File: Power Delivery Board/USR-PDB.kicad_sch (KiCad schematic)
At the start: 40 parts, among them U1 XT90, U10 Anderson PP45 Vert. 2x1, U11 Anderson PP45 Vert. 2x1, U12 Anderson PP45 Vert. 2x1, U13 TL2575HV-05IKV, U14 MCP3002-I/P, U2 Anderson PP45 Vert. 2x1, U3 Anderson PP45 Vert. 2x1, U4 Anderson PP45 Vert. 2x1, U5 Anderson PP45 Vert. 2x1, U6 Anderson PP45 Vert. 2x1, U7 LM2676T-12_NOPB

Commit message: traces added for the power delivery boards PCB
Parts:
- C1: footprint USR:CAP_WCAP-ATUL_05.0X11.0_WRE -> Capacitor_THT:CP_Radial_D10.0mm_P5.00mm
- C2, C6, C8: footprint USR:U2-K_NCH -> Capacitor_THT:CP_Radial_D10.0mm_P5.00mm
- C5: footprint USR:CAP_ATLL_06p3X15p0_WRE -> Capacitor_THT:CP_Radial_D10.0mm_P5.00mm
- C7: footprint USR:PCAP_6.3x7.7-ELECT_NCA -> Capacitor_THT:CP_Radial_D10.0mm_P5.00mm
- D1: footprint USR:SMA_DIO -> USR:DO-41_STM
- L1: footprint USR:IND_BOURNS_SRR1210 -> Inductor_THT:L_Axial_L5.3mm_D2.2mm_P10.16mm_Horizontal_Vishay_IM-1
- L2: footprint USR:IND_BOURNS_SDR1806 -> Inductor_THT:L_Axial_L7.0mm_D3.3mm_P12.70mm_Horizontal_Fastron_MICC
- L3: footprint USR:IND_BOURNS_SDR1806 -> Inductor_THT:L_Axial_L5.3mm_D2.2mm_P10.16mm_Horizontal_Vishay_IM-1
- U1: footprint (none) -> USR:AMASS_XT90PW-M_VERTICAL
- U15: footprint USR:JST-XA 2.54mm -> USR:JST-XA 4-PIN
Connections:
- no-connect marks 4 -> 16
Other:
- note removed: "create a vertical version of the AMASS_XT90PW-M for the hole sizes, reference the AMASS_XT30 vertical footprint for the layout we want"
- note removed: "find XT90 footprint"
- note removed: "use 10uH 0805 inductors, combine them into the 20uH inductor here"
- note removed: "use the 0805 SMD cap's we already have for the 100nF and 10nF cap's"
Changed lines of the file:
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@@
 		)
 	)
-	(text "use the 0805 SMD cap's we already have for \nthe 100nF and 10nF cap's"
-		(exclude_from_sim no)
-		(at 82.55 250.19 0)
-		(effects
-			(font
-				(size 1.27 1.27)
-			)
-		)
-	)
-	(text "find XT90 footprint"
-		(exclude_from_sim no)
-		(at 29.464 29.21 0)
-		(effects
-			(font
-				(size 1.27 1.27)
-			)
-		)
-	)
 	(text "3/12/2026"
 		(exclude_from_sim no)
@@
 		)
 	)
-	(text "create a vertical version of the AMASS_XT90PW-M for the hole \nsizes, reference the AMASS_XT30	vertical footprint for the\nlayout we want"
-		(exclude_from_sim no)
-		(at 78.232 32.258 0)
-		(effects
-			(font
-				(size 1.27 1.27)
-			)
-		)
-	)
 	(text "look into using JST 2.54mm XA male connectors for this"
 		(exclude_from_sim no)
@@
 		)
 	)
-	(text "use 10uH 0805 inductors, combine them into the \n20uH inductor here"
-		(exclude_from_sim no)
-		(at 373.888 186.436 0)
-		(effects
-			(font
-				(size 1.27 1.27)
-			)
-		)
-	)
 	(text "use the 3-pin JST-XA connectors to route 5V to the backplane"
 		(exclude_from_sim no)
@@
 	)
 	(no_connect
+		(at 147.32 86.36)
+	)
+	(no_connect
 		(at 135.89 220.98)
 	)
 	(no_connect
+		(at 168.91 86.36)
+	)
+	(no_connect
 		(at 152.4 101.6)
 	)
+	(no_connect
+		(at 147.32 83.82)
+	)
+	(no_connect
+		(at 147.32 36.83)
+	)
+	(no_connect
+		(at 168.91 83.82)
+	)
+	(no_connect
+		(at 147.32 41.91)
+	)
+	(no_connect
+		(at 168.91 39.37)
+	)
+	(no_connect
+		(at 147.32 39.37)
+	)
+	(no_connect
+		(at 147.32 81.28)
+	)
+	(no_connect
+		(at 168.91 81.28)
+	)
+	(no_connect
+		(at 168.91 41.91)
+	)
+	(no_connect
+		(at 168.91 36.83)
+	)
 	(wire
 		(pts
@@
 			)
 		)
-		(property "Footprint" "USR:CAP_ATLL_06p3X15p0_WRE"
+		(property "Footprint" "Capacitor_THT:CP_Radial_D10.0mm_P5.00mm"
 			(at 152.4 220.98 0)
 			(effects
@@
 			)
 		)
-		(property "Footprint" "USR:PCAP_6.3x7.7-ELECT_NCA"
+		(property "Footprint" "Capacitor_THT:CP_Radial_D10.0mm_P5.00mm"
 			(at 316.23 227.33 0)
 			(effects
@@
 			)
 		)
-		(property "Footprint" "USR:U2-K_NCH"
+		(property "Footprint" "Capacitor_THT:CP_Radial_D10.0mm_P5.00mm"
 			(at 63.5 228.6 0)
 			(effects
@@
 			)
 		)
-		(property "Footprint" "USR:CAP_WCAP-ATUL_05.0X11.0_WRE"
+		(property "Footprint" "Capacitor_THT:CP_Radial_D10.0mm_P5.00mm"
 			(at 63.5 217.17 0)
 			(effects
@@
 			)
 		)
-		(property "Footprint" "USR:U2-K_NCH"
+		(property "Footprint" "Capacitor_THT:CP_Radial_D10.0mm_P5.00mm"
 			(at 267.97 208.28 0)
 			(effects
@@
 			)
 		)
-		(property "Footprint" "USR:SMA_DIO"
+		(property "Footprint" "USR:DO-41_STM"
 			(at 88.9 232.41 0)
 			(effects
@@
 			)
 		)
-		(property "Footprint" "USR:U2-K_NCH"
+		(property "Footprint" "Capacitor_THT:CP_Radial_D10.0mm_P5.00mm"
 			(at 375.92 220.98 0)
 			(effects
@@
 			)
 		)
-		(property "Footprint" "USR:IND_BOURNS_SDR1806"
+		(property "Footprint" "Inductor_THT:L_Axial_L7.0mm_D3.3mm_P12.70mm_Horizontal_Fastron_MICC"
 			(at 287.02 215.9 0)
 			(effects
@@
 			)
 		)
-		(property "Footprint" ""
+		(property "Footprint" "USR:AMASS_XT90PW-M_VERTICAL"
 			(at 29.21 45.72 0)
 			(effects
@@
 			)
 		)
-		(property "Footprint" "USR:IND_BOURNS_SRR1210"
+		(property "Footprint" "Inductor_THT:L_Axial_L5.3mm_D2.2mm_P10.16mm_Horizontal_Vishay_IM-1"
 			(at 147.32 210.82 0)
 			(effects
@@
 			)
 		)
-		(property "Footprint" "USR:IND_BOURNS_SDR1806"
+		(property "Footprint" "Inductor_THT:L_Axial_L5.3mm_D2.2mm_P10.16mm_Horizontal_Vishay_IM-1"
 			(at 298.45 215.9 0)
 			(effects
@@
 			)
 		)
-		(property "Footprint" "USR:JST-XA 2.54mm"
+		(property "Footprint" "USR:JST-XA 4-PIN"
 			(at 375.92 53.34 0)
 			(effects

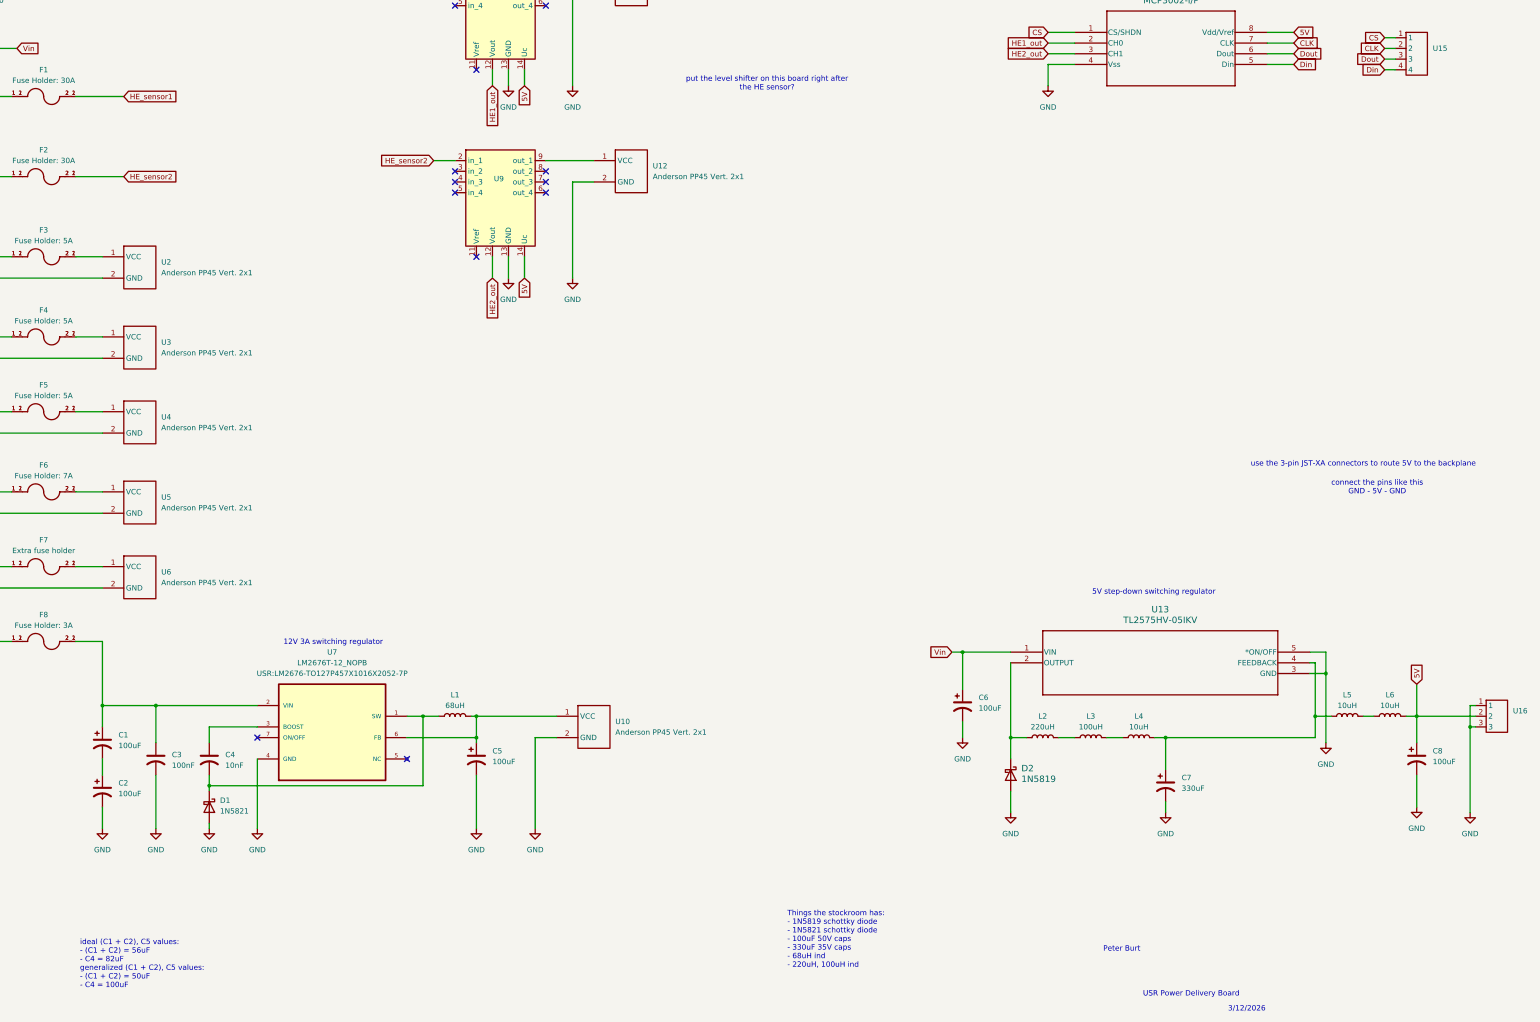
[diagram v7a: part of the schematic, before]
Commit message: Update PDB with easier-to-obtain components
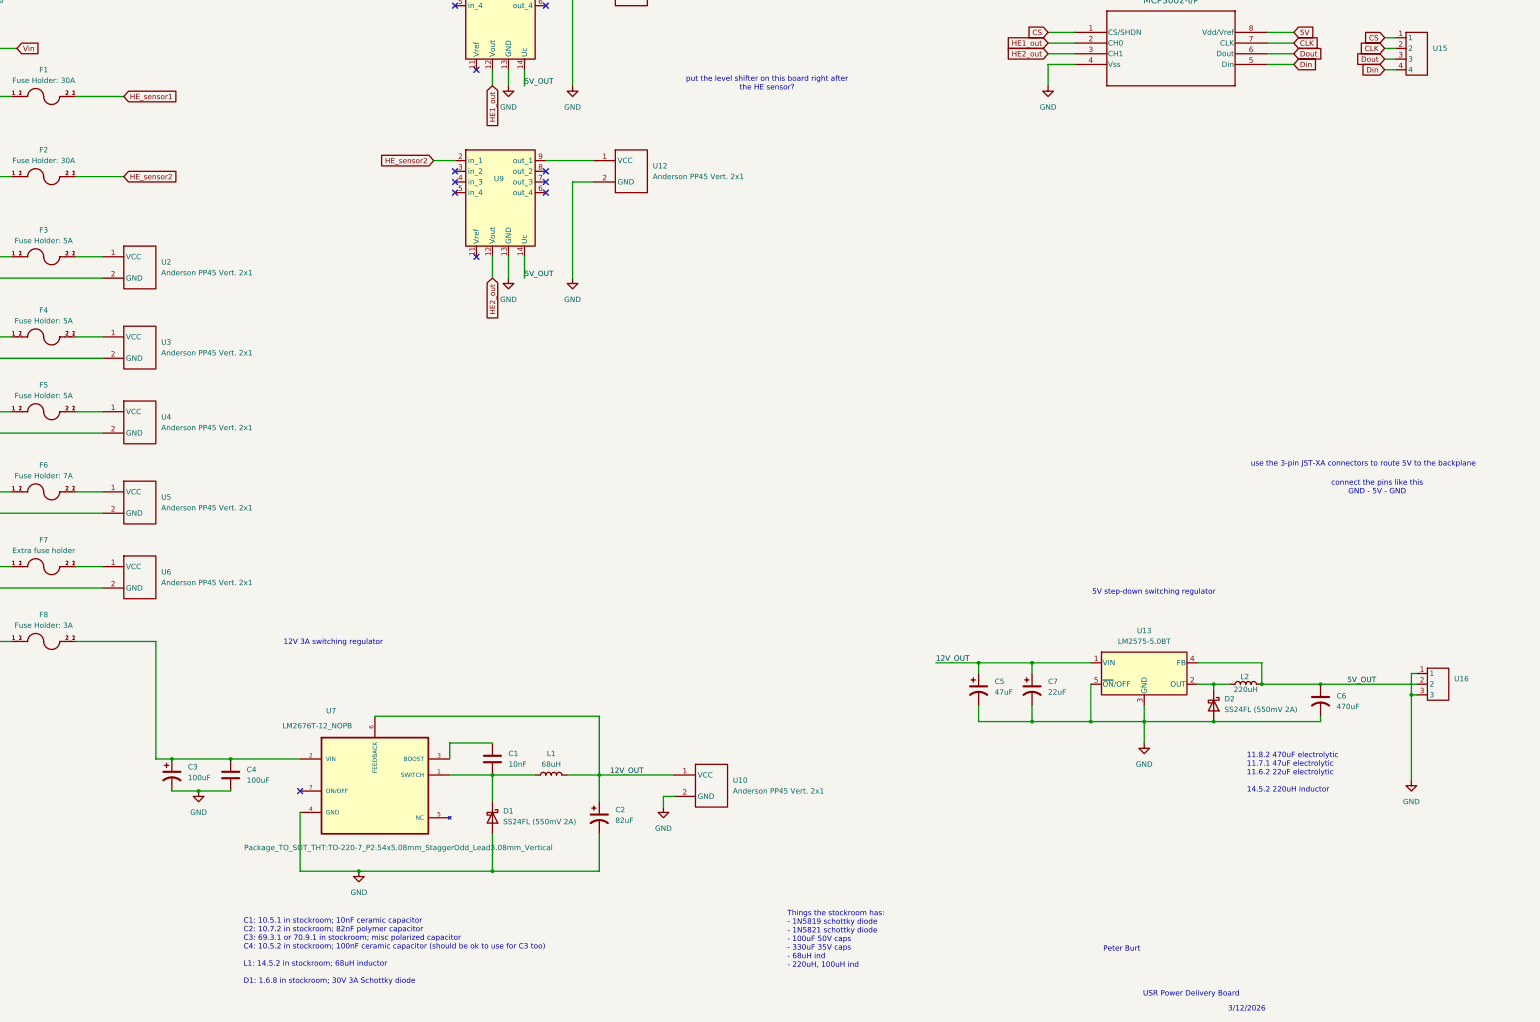
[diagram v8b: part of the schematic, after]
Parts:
- removed C1, C6, C8: 100uF, Capacitor_THT:CP_Radial_D10.0mm_P5.00mm, symbol Device:C_Polarized_US
- removed C3: 100nF, Capacitor_SMD:C_0805_2012Metric_Pad1.18x1.45mm_HandSolder, symbol Device:C_US
- removed C4: 10nF, Capacitor_SMD:C_0805_2012Metric_Pad1.18x1.45mm_HandSolder, symbol Device:C_US
- removed L3: 100uH, Inductor_THT:L_Axial_L5.3mm_D2.2mm_P10.16mm_Horizontal_Vishay_IM-1, symbol Device:L
- removed L4, L5, L6: 10uH, Inductor_SMD:L_0805_2012Metric_Pad1.05x1.20mm_HandSolder, symbol Device:L
- removed U13: TL2575HV-05IKV, USR:TL2575HV-05IKV, symbol USR_SymLibrary:TL2575HV-05IKV
- removed U7: LM2676T-12_NOPB, USR:LM2676-TO127P457X1016X2052-7P, symbol USR_SymLibrary:LM2676T-12_NOPB
- added C1: 10nF, Capacitor_THT:C_Disc_D16.0mm_W5.0mm_P10.00mm, symbol Device:C
- added C3: 100uF, Capacitor_THT:CP_Radial_D8.0mm_P3.50mm, symbol Device:C_Polarized_US
- added C4: 100uF, Capacitor_THT:C_Disc_D16.0mm_W5.0mm_P10.00mm, symbol Device:C
- added C6: 470uF, Capacitor_THT:CP_Radial_D8.0mm_P3.50mm, symbol Device:C_US
- added U13: LM2575-5.0BT, Package_TO_SOT_THT:TO-220-5_Vertical, symbol Regulator_Switching:LM2575-5.0BT
- added U7: LM2676T-12_NOPB, Package_TO_SOT_THT:TO-220-7_P2.54x5.08mm_StaggerOdd_Lead3.08mm_Vertical, symbol USR:LM2676T-12_NOPB
- C2: value 100uF -> 82uF; footprint Capacitor_THT:CP_Radial_D10.0mm_P5.00mm -> Capacitor_THT:CP_Radial_D8.0mm_P3.50mm
- C5: value 100uF -> 47uF; footprint Capacitor_THT:CP_Radial_D10.0mm_P5.00mm -> Capacitor_THT:CP_Radial_D8.0mm_P3.50mm
- C7: value 330uF -> 22uF; footprint Capacitor_THT:CP_Radial_D10.0mm_P5.00mm -> Capacitor_THT:CP_Radial_D8.0mm_P3.50mm
- D1: value 1N5821 -> SS24FL (550mV 2A); footprint USR:DO-41_STM -> Diode_THT:D_DO-41_SOD81_P10.16mm_Horizontal
- D2: value 1N5819 -> SS24FL (550mV 2A); footprint USR:DO-41_STM -> Diode_THT:D_DO-41_SOD81_P10.16mm_Horizontal
- L2: footprint Inductor_THT:L_Axial_L7.0mm_D3.3mm_P12.70mm_Horizontal_Fastron_MICC -> Inductor_THT:L_Axial_L5.3mm_D2.2mm_P10.16mm_Horizontal_Vishay_IM-1
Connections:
- net 5V: no longer U16.2, U8.14 (Uc), U9.14 (Uc)
- net GND: now also C3.2, C4.2, C6.2, U13.3 (GND), U13.5 (~{ON}/OFF), U7.4 (GND)
- net 12V_OUT: now reaches C5.1, L1.2, U10.1 (VCC)
- net 12V_OUT: now also C2.1, C7.1, U13.1 (VIN), U7.6 (FEEDBACK)
- net at D2.1 (K), L2.1: now also U13.2 (OUT)
- net at D1.1 (K), L1.1: now also C1.2, U7.1 (SWITCH)
- net at F8.2_1, F8.2_2: now also C3.1, C4.1, U7.2 (VIN)
- net 5V_OUT: now reaches L2.2
- net 5V_OUT: now also U16.2, U8.14 (Uc), U9.14 (Uc), C6.1, U13.4 (FB)
- new net: C1.1, U7.3 (BOOST)
- no-connect marks 16 -> 15
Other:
- note added: "11.8.2 470uF electrolytic 11.7.1 47uF electrolytic 11.6.2 22uF electrolytic 14.5.2 220uH inductor"
- note added: "C1: 10.5.1 in stockroom; 10nF ceramic capacitor C2: 10.7.2 in stockroom; 82nF polymer capacitor C3: 69.3.1 or 70.9.1 in stockroom; misc polarized capacitor C4: 10.5.2 in stockroom; 100nF ceramic capacitor (should be ok to use for C3 too) L1: 14.5.2 in stockroom; 68uH inductor D1: 1.6.8 in stockroom; 30V 3A Schottky diode"
- note removed: "ideal (C1 + C2), C5 values: - (C1 + C2) = 56uF - C4 = 82uF generalized (C1 + C2), C5 values: - (C1 + C2) = 50uF - C4 = 100uF"
- moved on the sheet: U10, U16
